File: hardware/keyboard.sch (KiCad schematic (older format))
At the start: 19 parts, among them J1 USB_OTG, J2 CONN_02X10, U1 ATMEGA32U4-AU, Y1 16MHz

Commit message: Update parts after starting sourcing
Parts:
- D101: footprint LEDs:LED_RGB_5050-6 -> LEDs:LED_RGB_PLCC-6
- Y1: footprint Crystals:Crystal_SMD_2012-2pin_2.0x1.2mm_HandSoldering -> Crystals:Crystal_SMD_3225-4pin_3.2x2.5mm_HandSoldering
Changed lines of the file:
@@
 F 0 "Y1" H 2600 1950 50  0000 C CNN
 F 1 "16MHz" H 2600 1750 50  0000 C CNN
-F 2 "Crystals:Crystal_SMD_2012-2pin_2.0x1.2mm_HandSoldering" H 2600 1850 50  0001 C CNN
+F 2 "Crystals:Crystal_SMD_3225-4pin_3.2x2.5mm_HandSoldering" H 2600 1850 50  0001 C CNN
 F 3 "" H 2600 1850 50  0001 C CNN
 	1    2600 1850
@@
 F 0 "D101" H 6900 2097 50  0000 C CNN
 F 1 "LED_RGB" H 6900 2006 50  0000 C CNN
-F 2 "LEDs:LED_RGB_5050-6" H 6900 1550 50  0001 C CNN
+F 2 "LEDs:LED_RGB_PLCC-6" H 6900 1550 50  0001 C CNN
 F 3 "" H 6900 1550 50  0001 C CNN
 	1    6900 1600

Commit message: WIP for V2 fixes
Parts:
- removed J2: CONN_02X10, keyboard-modules:ExpansionPads, symbol CONN_02X10
- added J10, J11, J12, J13, J14, J2, J3, J4, J5, J6, J7, J8, J9: CONN_01X01, keyboard-modules:CONN_1, symbol CONN_01X01
- J1: footprint Connectors_USB:USB_Micro-B_Molex-105017-0001 -> keyboard-modules:USB-MINI
- Y1: footprint Crystals:Crystal_SMD_3225-4pin_3.2x2.5mm_HandSoldering -> Crystals:Crystal_Round_d1.0mm_Vertical
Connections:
- net labels removed: VCC
- wire segments 44 -> 40

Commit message: More WIP on V2
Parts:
- F1: footprint Fuse_Holders_and_Fuses:Fuse_SMD1206_HandSoldering -> Resistors_SMD:R_1206_HandSoldering
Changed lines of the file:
@@
 LIBS:valves
 LIBS:keyboard-cache
-EELAYER 25 0
+EELAYER 26 0
 EELAYER END
 $Descr A4 11693 8268
@@
 F 0 "F1" V 1975 2500 50  0000 C CNN
 F 1 "Polyfuse_Small" V 2125 2500 50  0000 C CNN
-F 2 "Fuse_Holders_and_Fuses:Fuse_SMD1206_HandSoldering" H 2100 2300 50  0001 L CNN
+F 2 "Resistors_SMD:R_1206_HandSoldering" H 2100 2300 50  0001 L CNN
 F 3 "" H 2050 2500 50  0001 C CNN
 	1    2050 2500

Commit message: Add more mounting holes, re-route updated components
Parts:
- removed D101: LED_RGB, LEDs:LED_RGB_PLCC-6, symbol LED_RGB
- removed J10, J11, J12, J13, J14, J2, J3, J4, J5, J6, J8, J9: CONN_01X01, keyboard-modules:CONN_1, symbol CONN_01X01
- removed R1, R3: 1k, Resistors_SMD:R_1206_HandSoldering, symbol R
- added D65: LED_CRGB, LEDs:LED_D5.0mm-4, symbol LED_CRGB
- added GND1, PD2, PD3, PD4, PD5, PD6, PE6, PF0, PF1, PF4, PF5, PF6, PF7, SCL1, SDA1, VCC1: CONN_01X01, keyboard-modules:CONN_1, symbol CONN_01X01
- renumbered J7 to PB7
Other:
- moved on the sheet: PB7

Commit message: finish V2
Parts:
- removed D65: LED_CRGB, LEDs:LED_D5.0mm-4, symbol LED_CRGB
- added D99: LED_ARGB, LEDs:LED_D5.0mm-4-v2, symbol LED_ARGB
- added R1, R3: 1k, Resistors_SMD:R_1206_HandSoldering, symbol R
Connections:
- net +5V: now also D99.1 (A)
- net GND: no longer R2.2
- net LED1: now also R1.2
- net LED2: now also R2.2
- net LED3: now also R3.2
- net at R2.1: now also D99.3 (GK)
- new net: D99.2 (RK), R1.1
- new net: D99.4 (BK), R3.1
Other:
- moved on the sheet: R2
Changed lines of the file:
@@
-$EndComp
-$Comp
-L GND #PWR08
-U 1 1 594E9E01
-P 6400 1600
-F 0 "#PWR08" H 6400 1350 50  0001 C CNN
-F 1 "GND" H 6400 1450 50  0000 C CNN
-F 2 "" H 6400 1600 50  0001 C CNN
-F 3 "" H 6400 1600 50  0001 C CNN
-	1    6400 1600
-	1    0    0    -1
 $EndComp
 $Comp
 L R R2
 U 1 1 594E9E0D
-P 6550 1600
-F 0 "R2" V 6630 1600 50  0000 C CNN
-F 1 "1k" V 6550 1600 50  0000 C CNN
-F 2 "Resistors_SMD:R_1206_HandSoldering" V 6480 1600 50  0001 C CNN
-F 3 "" H 6550 1600 50  0001 C CNN
-	1    6550 1600
+P 6050 1250
+F 0 "R2" V 6130 1250 50  0000 C CNN
+F 1 "1k" V 6050 1250 50  0000 C CNN
+F 2 "Resistors_SMD:R_1206_HandSoldering" V 5980 1250 50  0001 C CNN
+F 3 "" H 6050 1250 50  0001 C CNN
+	1    6050 1250
 	0    1    1    0
 $EndComp
-Text GLabel 7100 1400 2    60   Input ~ 0
+Text GLabel 5900 1050 0    60   Input ~ 0
 LED1
-Text GLabel 7100 1600 2    60   Input ~ 0
+Text GLabel 5900 1250 0    60   Input ~ 0
 LED2
 $Comp
@@
 	5050 3450 5250 3450
 $Comp
-L GND #PWR09
+L GND #PWR08
 U 1 1 594EA1C7
 P 6150 3450
-F 0 "#PWR09" H 6150 3200 50  0001 C CNN
+F 0 "#PWR08" H 6150 3200 50  0001 C CNN
 F 1 "GND" H 6150 3300 50  0000 C CNN
 F 2 "" H 6150 3450 50  0001 C CNN
@@
 	5550 3450 6150 3450
 $Comp
-L GND #PWR010
+L GND #PWR09
 U 1 1 594EA3EB
 P 2050 1350
-F 0 "#PWR010" H 2050 1100 50  0001 C CNN
+F 0 "#PWR09" H 2050 1100 50  0001 C CNN
 F 1 "GND" H 2050 1200 50  0000 C CNN
 F 2 "" H 2050 1350 50  0001 C CNN
@@
 $EndComp
 $Comp
-L +5V #PWR011
+L +5V #PWR010
 U 1 1 5955BD4A
 P 1800 800
-F 0 "#PWR011" H 1800 650 50  0001 C CNN
+F 0 "#PWR010" H 1800 650 50  0001 C CNN
 F 1 "+5V" H 1800 940 50  0000 C CNN
 F 2 "" H 1800 800 50  0001 C CNN
@@
 $EndComp
 $Comp
-L GND #PWR012
+L GND #PWR011
 U 1 1 5955BE42
 P 1800 1000
-F 0 "#PWR012" H 1800 750 50  0001 C CNN
+F 0 "#PWR011" H 1800 750 50  0001 C CNN
 F 1 "GND" H 1800 850 50  0000 C CNN
 F 2 "" H 1800 1000 50  0001 C CNN
@@
 	1    0    0    -1
 $EndComp
-Text GLabel 7100 1800 2    60   Input ~ 0
+Text GLabel 5900 1450 0    60   Input ~ 0
 LED3
 Text GLabel 5050 1850 2    60   Input ~ 0
@@
 $EndComp
 $Comp
-L LED_CRGB D65
-U 1 1 5A0960D5
-P 6900 1600
-F 0 "D65" H 6900 1970 50  0000 C CNN
-F 1 "LED_CRGB" H 6900 1250 50  0000 C CNN
-F 2 "LEDs:LED_D5.0mm-4" H 6900 1550 50  0001 C CNN
-F 3 "" H 6900 1550 50  0001 C CNN
-	1    6900 1600
-	1    0    0    -1
-$EndComp
-$Comp
 L CONN_01X01 PD6
 U 1 1 5A09791E
@@
 	1    0    0    -1
 $EndComp
-Connection ~ 9450 2350
 Connection ~ 5600 2450
+$Comp
+L LED_ARGB D99
+U 1 1 5A1A0698
+P 6400 1250
+F 0 "D99" H 6400 1620 50  0000 C CNN
+F 1 "LED_ARGB" H 6400 900 50  0000 C CNN
+F 2 "LEDs:LED_D5.0mm-4-v2" H 6400 1200 50  0001 C CNN
+F 3 "" H 6400 1200 50  0001 C CNN
+	1    6400 1250
+	1    0    0    -1
+$EndComp
+$Comp
+L R R1
+U 1 1 5A1A082F
+P 6050 1050
+F 0 "R1" V 6130 1050 50  0000 C CNN
+F 1 "1k" V 6050 1050 50  0000 C CNN
+F 2 "Resistors_SMD:R_1206_HandSoldering" V 5980 1050 50  0001 C CNN
+F 3 "" H 6050 1050 50  0001 C CNN
+	1    6050 1050
+	0    1    1    0
+$EndComp
+$Comp
+L R R3
+U 1 1 5A1A08BC
+P 6050 1450
+F 0 "R3" V 6130 1450 50  0000 C CNN
+F 1 "1k" V 6050 1450 50  0000 C CNN
+F 2 "Resistors_SMD:R_1206_HandSoldering" V 5980 1450 50  0001 C CNN
+F 3 "" H 6050 1450 50  0001 C CNN
+	1    6050 1450
+	0    1    1    0
+$EndComp
+$Comp
+L +5V #PWR012
+U 1 1 5A1A091A
+P 6600 1250
+F 0 "#PWR012" H 6600 1100 50  0001 C CNN
+F 1 "+5V" H 6600 1390 50  0000 C CNN
+F 2 "" H 6600 1250 50  0001 C CNN
+F 3 "" H 6600 1250 50  0001 C CNN
+	1    6600 1250
+	1    0    0    -1
+$EndComp
 $EndSCHEMATC

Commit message: Update schematic, WIP fixes + adding test points
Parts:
- removed GND1, PB7, PD2, PD3, PD4, PD5, PD6, PE6, PF0, PF1, PF4, PF5, PF6, PF7, SCL1, SDA1, VCC1: CONN_01X01, keyboard-modules:CONN_1, symbol CONN_01X01
- added J2: CONN_01X05, Pin_Headers:Pin_Header_Straight_1x05_Pitch1.27mm, symbol CONN_01X05
- added J3: CONN_01X04, Pin_Headers:Pin_Header_Straight_1x04_Pitch1.27mm, symbol CONN_01X04
- added J4: CONN_01X07, Pin_Headers:Pin_Header_Straight_1x07_Pitch1.27mm, symbol CONN_01X07
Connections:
- net +5V: now also J3.1 (P1), J4.1 (P1)
- net GND: now also J3.4 (P4), J4.7 (P7)
- net LED1: now also U1.28 ((ADC11/PCINT4)PB4); no longer U1.29 ((ADC12/OC1A/~OC4B~/PCINT12)PB5)
- net LED2: now also U1.29 ((ADC12/OC1A/~OC4B~/PCINT12)PB5); no longer U1.30 ((ADC13/OC1B/OC4B/PCINT13)PB6)
- net LED3: now also U1.30 ((ADC13/OC1B/OC4B/PCINT13)PB6); no longer U1.27 ((T0/OC4D/ADC10)PD7)
- net PF4: now also J4.3 (P3)
- net PF5: now also J4.4 (P4)
- net PF6: now also J4.5 (P5)
- net PF7: now also J4.6 (P6)
- net ROW0: now also J2.1 (P1)
- net ROW1: now also J2.2 (P2)
- net ROW2: now also J2.3 (P3)
- net ROW3: now also J2.4 (P4)
- net ROW4: now also U1.12 ((OC0A/OC1C/~RTS~/PCINT7)PB7), J2.5 (P5); no longer U1.28 ((ADC11/PCINT4)PB4)
- net SCL: now also J3.2 (P2)
- net SDA: now also J3.3 (P3)
- net RESET: now reaches S100.2, U1.13 (~RESET~)
- net RESET: now also J4.2 (P2)
- net PE2: now reaches R8.2, U1.33 ((~HWB~)PE2)
- new net PD7: U1.27 ((T0/OC4D/ADC10)PD7)
- no-connect marks 0 -> 3
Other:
- moved on the sheet: R4, R5, S100

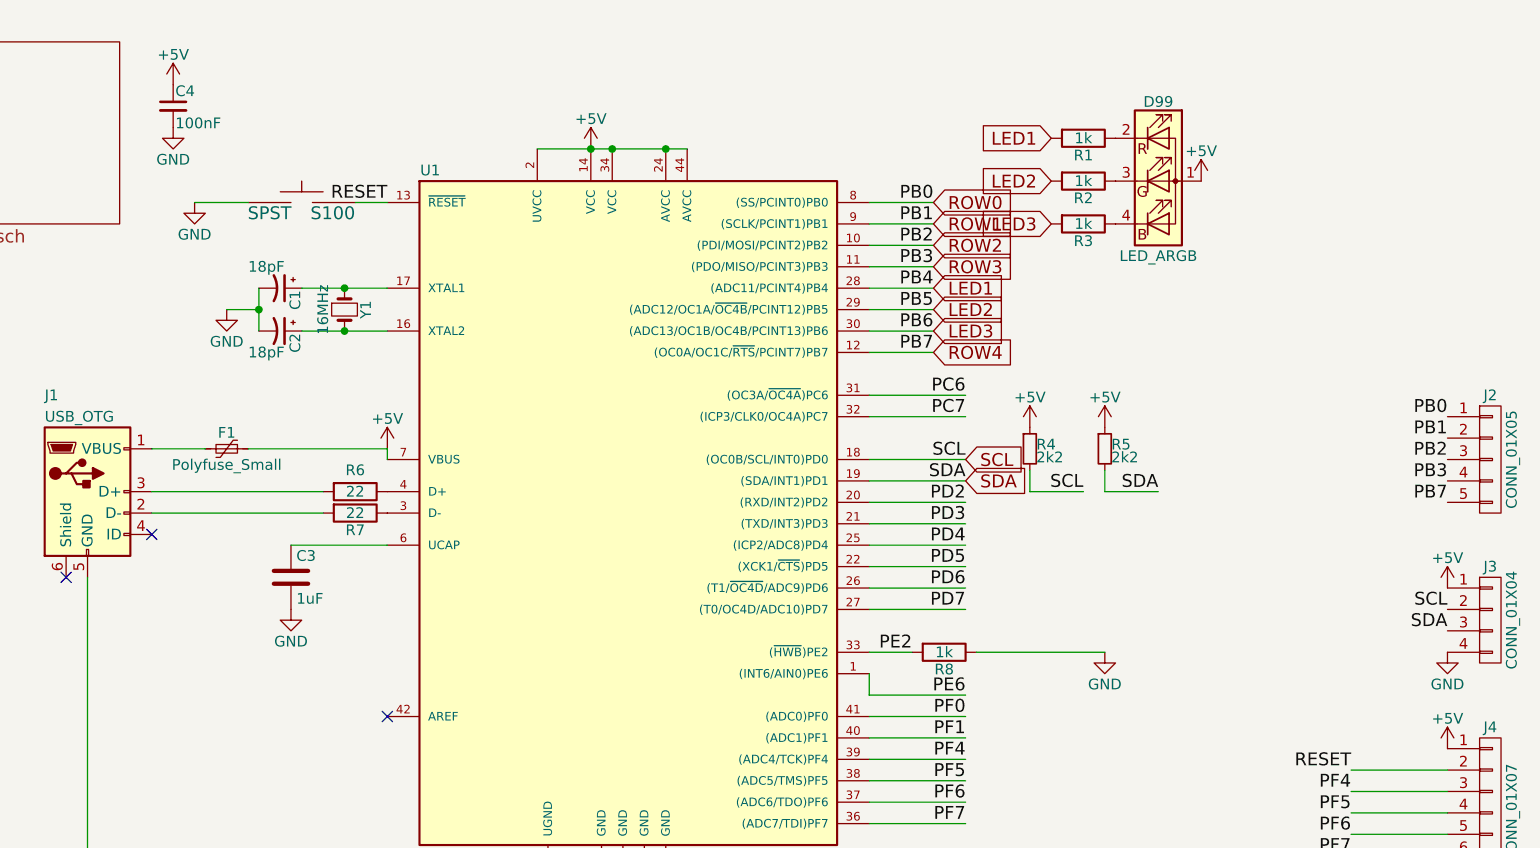
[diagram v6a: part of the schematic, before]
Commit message: PCB revisions - more test points and fixes
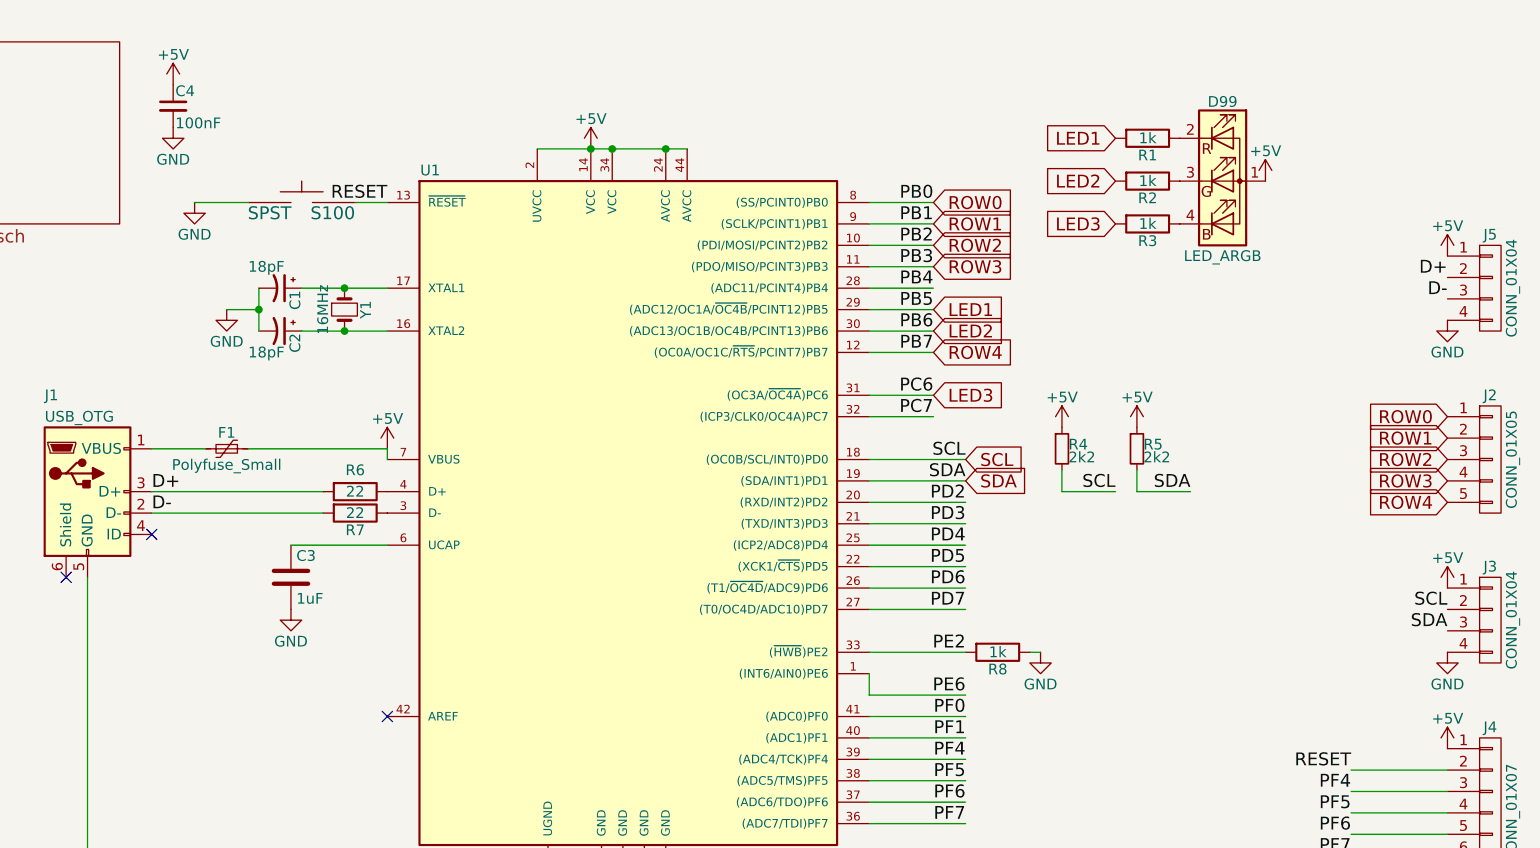
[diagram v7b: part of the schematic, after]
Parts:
- added J5: CONN_01X04, Pin_Headers:Pin_Header_Straight_1x04_Pitch1.27mm, symbol CONN_01X04
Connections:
- net PC6 is gone; now on net LED3: U1.31 ((OC3A/~OC4A~)PC6)
- net +5V: now also J5.1 (P1)
- net GND: now also J5.4 (P4)
- net LED1: now also U1.29 ((ADC12/OC1A/~OC4B~/PCINT12)PB5); no longer U1.28 ((ADC11/PCINT4)PB4)
- net LED2: now also U1.30 ((ADC13/OC1B/OC4B/PCINT13)PB6); no longer U1.29 ((ADC12/OC1A/~OC4B~/PCINT12)PB5)
- net LED3: no longer U1.30 ((ADC13/OC1B/OC4B/PCINT13)PB6)
- net D-: now reaches J1.2 (D-), R7.2
- net D-: now also J5.3 (P3)
- net D+: now reaches J1.3 (D+), R6.2
- net D+: now also J5.2 (P2)
- new net PB4: U1.28 ((ADC11/PCINT4)PB4)
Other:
- moved on the sheet: D99, R1, R2, R3, R4, R5, R8
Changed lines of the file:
@@
 EESchema Schematic File Version 2
-LIBS:keyboard-rescue
 LIBS:power
 LIBS:device
@@
 L R_Small R5
 U 1 1 594E97F5
-P 6150 2500
-F 0 "R5" H 6180 2520 50  0000 L CNN
-F 1 "2k2" H 6180 2460 50  0000 L CNN
-F 2 "Resistors_SMD:R_1206_HandSoldering" H 6150 2500 50  0001 C CNN
-F 3 "" H 6150 2500 50  0001 C CNN
-	1    6150 2500
+P 6300 2500
+F 0 "R5" H 6330 2520 50  0000 L CNN
+F 1 "2k2" H 6330 2460 50  0000 L CNN
+F 2 "Resistors_SMD:R_1206_HandSoldering" H 6300 2500 50  0001 C CNN
+F 3 "" H 6300 2500 50  0001 C CNN
+	1    6300 2500
 	1    0    0    -1
 $EndComp
@@
 L R_Small R4
 U 1 1 594E9840
-P 5800 2500
-F 0 "R4" H 5830 2520 50  0000 L CNN
-F 1 "2k2" H 5830 2460 50  0000 L CNN
-F 2 "Resistors_SMD:R_1206_HandSoldering" H 5800 2500 50  0001 C CNN
-F 3 "" H 5800 2500 50  0001 C CNN
-	1    5800 2500
+P 5950 2500
+F 0 "R4" H 5980 2520 50  0000 L CNN
+F 1 "2k2" H 5980 2460 50  0000 L CNN
+F 2 "Resistors_SMD:R_1206_HandSoldering" H 5950 2500 50  0001 C CNN
+F 3 "" H 5950 2500 50  0001 C CNN
+	1    5950 2500
 	1    0    0    -1
 $EndComp
@@
 L +5V #PWR06
 U 1 1 594E98E9
-P 5800 2400
-F 0 "#PWR06" H 5800 2250 50  0001 C CNN
-F 1 "+5V" H 5800 2540 50  0000 C CNN
-F 2 "" H 5800 2400 50  0001 C CNN
-F 3 "" H 5800 2400 50  0001 C CNN
-	1    5800 2400
+P 5950 2400
+F 0 "#PWR06" H 5950 2250 50  0001 C CNN
+F 1 "+5V" H 5950 2540 50  0000 C CNN
+F 2 "" H 5950 2400 50  0001 C CNN
+F 3 "" H 5950 2400 50  0001 C CNN
+	1    5950 2400
 	1    0    0    -1
 $EndComp
@@
 L +5V #PWR07
 U 1 1 594E9917
-P 6150 2400
-F 0 "#PWR07" H 6150 2250 50  0001 C CNN
-F 1 "+5V" H 6150 2540 50  0000 C CNN
-F 2 "" H 6150 2400 50  0001 C CNN
-F 3 "" H 6150 2400 50  0001 C CNN
-	1    6150 2400
+P 6300 2400
+F 0 "#PWR07" H 6300 2250 50  0001 C CNN
+F 1 "+5V" H 6300 2540 50  0000 C CNN
+F 2 "" H 6300 2400 50  0001 C CNN
+F 3 "" H 6300 2400 50  0001 C CNN
+	1    6300 2400
 	1    0    0    -1
 $EndComp
@@
 L R R2
 U 1 1 594E9E0D
-P 6050 1250
-F 0 "R2" V 6130 1250 50  0000 C CNN
-F 1 "1k" V 6050 1250 50  0000 C CNN
-F 2 "Resistors_SMD:R_1206_HandSoldering" V 5980 1250 50  0001 C CNN
-F 3 "" H 6050 1250 50  0001 C CNN
-	1    6050 1250
-	0    1    1    0
-$EndComp
-Text GLabel 5900 1050 0    60   Input ~ 0
+P 6350 1250
+F 0 "R2" V 6430 1250 50  0000 C CNN
+F 1 "1k" V 6350 1250 50  0000 C CNN
+F 2 "Resistors_SMD:R_1206_HandSoldering" V 6280 1250 50  0001 C CNN
+F 3 "" H 6350 1250 50  0001 C CNN
+	1    6350 1250
+	0    1    1    0
+$EndComp
+Text GLabel 6200 1050 0    60   Input ~ 0
 LED1
-Text GLabel 5900 1250 0    60   Input ~ 0
+Text GLabel 6200 1250 0    60   Input ~ 0
 LED2
 $Comp
 L R R8
 U 1 1 594EA13B
-P 5400 3450
-F 0 "R8" V 5480 3450 50  0000 C CNN
-F 1 "1k" V 5400 3450 50  0000 C CNN
-F 2 "Resistors_SMD:R_1206_HandSoldering" V 5330 3450 50  0001 C CNN
-F 3 "" H 5400 3450 50  0001 C CNN
-	1    5400 3450
-	0    1    1    0
-$EndComp
-Wire Wire Line
-	5050 3450 5250 3450
+P 5650 3450
+F 0 "R8" V 5730 3450 50  0000 C CNN
+F 1 "1k" V 5650 3450 50  0000 C CNN
+F 2 "Resistors_SMD:R_1206_HandSoldering" V 5580 3450 50  0001 C CNN
+F 3 "" H 5650 3450 50  0001 C CNN
+	1    5650 3450
+	0    1    1    0
+$EndComp
+Wire Wire Line
+	5050 3450 5500 3450
 $Comp
 L GND #PWR08
 U 1 1 594EA1C7
-P 6150 3450
-F 0 "#PWR08" H 6150 3200 50  0001 C CNN
-F 1 "GND" H 6150 3300 50  0000 C CNN
-F 2 "" H 6150 3450 50  0001 C CNN
-F 3 "" H 6150 3450 50  0001 C CNN
-	1    6150 3450
-	1    0    0    -1
-$EndComp
-Wire Wire Line
-	5550 3450 6150 3450
+P 5850 3450
+F 0 "#PWR08" H 5850 3200 50  0001 C CNN
+F 1 "GND" H 5850 3300 50  0000 C CNN
+F 2 "" H 5850 3450 50  0001 C CNN
+F 3 "" H 5850 3450 50  0001 C CNN
+	1    5850 3450
+	1    0    0    -1
+$EndComp
+Wire Wire Line
+	5800 3450 5850 3450
 $Comp
 L GND #PWR09
@@
 	2150 1350 1900 1350
 Wire Wire Line
-	5050 2250 5500 2250
-Wire Wire Line
-	5050 2350 5500 2350
-Wire Wire Line
 	5050 2750 5500 2750
 Wire Wire Line
@@
 Wire Wire Line
 	7300 4400 7750 4400
-Text Label 5500 2250 2    60   ~ 0
+Text Label 5350 2250 2    60   ~ 0
 PC6
-Text Label 5500 2350 2    60   ~ 0
+Text Label 5350 2350 2    60   ~ 0
 PC7
 Text Label 5500 2750 2    60   ~ 0
@@
 	1    0    0    -1
 $EndComp
-Text GLabel 5900 1450 0    60   Input ~ 0
+Text GLabel 6200 1450 0    60   Input ~ 0
 LED3
-Text GLabel 5350 1750 2    60   Input ~ 0
+Text GLabel 5350 1850 2    60   Input ~ 0
 LED1
-Text GLabel 5350 1850 2    60   Input ~ 0
+Text GLabel 5350 1950 2    60   Input ~ 0
 LED2
-Text GLabel 5350 1950 2    60   Input ~ 0
+Text GLabel 5350 2250 2    60   Input ~ 0
 LED3
 $Comp
 L LED_ARGB D99
 U 1 1 5A1A0698
-P 6400 1250
-F 0 "D99" H 6400 1620 50  0000 C CNN
-F 1 "LED_ARGB" H 6400 900 50  0000 C CNN
-F 2 "LEDs:LED_D5.0mm-4-v2" H 6400 1200 50  0001 C CNN
-F 3 "" H 6400 1200 50  0001 C CNN
-	1    6400 1250
+P 6700 1250
+F 0 "D99" H 6700 1620 50  0000 C CNN
+F 1 "LED_ARGB" H 6700 900 50  0000 C CNN
+F 2 "LEDs:LED_D5.0mm-4-v2" H 6700 1200 50  0001 C CNN
+F 3 "" H 6700 1200 50  0001 C CNN
+	1    6700 1250
 	1    0    0    -1
 $EndComp
@@
 L R R1
 U 1 1 5A1A082F
-P 6050 1050
-F 0 "R1" V 6130 1050 50  0000 C CNN
-F 1 "1k" V 6050 1050 50  0000 C CNN
-F 2 "Resistors_SMD:R_1206_HandSoldering" V 5980 1050 50  0001 C CNN
-F 3 "" H 6050 1050 50  0001 C CNN
-	1    6050 1050
+P 6350 1050
+F 0 "R1" V 6430 1050 50  0000 C CNN
+F 1 "1k" V 6350 1050 50  0000 C CNN
+F 2 "Resistors_SMD:R_1206_HandSoldering" V 6280 1050 50  0001 C CNN
+F 3 "" H 6350 1050 50  0001 C CNN
+	1    6350 1050
 	0    1    1    0
 $EndComp
@@
 L R R3
 U 1 1 5A1A08BC
-P 6050 1450
-F 0 "R3" V 6130 1450 50  0000 C CNN
-F 1 "1k" V 6050 1450 50  0000 C CNN
-F 2 "Resistors_SMD:R_1206_HandSoldering" V 5980 1450 50  0001 C CNN
-F 3 "" H 6050 1450 50  0001 C CNN
-	1    6050 1450
+P 6350 1450
+F 0 "R3" V 6430 1450 50  0000 C CNN
+F 1 "1k" V 6350 1450 50  0000 C CNN
+F 2 "Resistors_SMD:R_1206_HandSoldering" V 6280 1450 50  0001 C CNN
+F 3 "" H 6350 1450 50  0001 C CNN
+	1    6350 1450
 	0    1    1    0
 $EndComp
@@
 L +5V #PWR012
 U 1 1 5A1A091A
-P 6600 1250
-F 0 "#PWR012" H 6600 1100 50  0001 C CNN
-F 1 "+5V" H 6600 1390 50  0000 C CNN
-F 2 "" H 6600 1250 50  0001 C CNN
-F 3 "" H 6600 1250 50  0001 C CNN
-	1    6600 1250
+P 6900 1250
+F 0 "#PWR012" H 6900 1100 50  0001 C CNN
+F 1 "+5V" H 6900 1390 50  0000 C CNN
+F 2 "" H 6900 1250 50  0001 C CNN
+F 3 "" H 6900 1250 50  0001 C CNN
+	1    6900 1250
 	1    0    0    -1
 $EndComp
@@
 Text Label 5500 3950 2    60   ~ 0
 PF4
-Text Label 5250 3450 2    60   ~ 0
+Text Label 5500 3450 2    60   ~ 0
 PE2
 Wire Wire Line
@@
 SDA
 Wire Wire Line
-	5800 2600 5800 2700
-Wire Wire Line
-	5800 2700 6050 2700
-Text Label 6050 2700 2    60   ~ 0
+	5950 2600 5950 2700
+Wire Wire Line
+	5950 2700 6200 2700
+Text Label 6200 2700 2    60   ~ 0
 SCL
 Wire Wire Line
-	6400 2700 6150 2700
-Wire Wire Line
-	6150 2700 6150 2600
-Text Label 6400 2700 2    60   ~ 0
+	6550 2700 6300 2700
+Wire Wire Line
+	6300 2700 6300 2600
+Text Label 6550 2700 2    60   ~ 0
 SDA
 Wire Wire Line
@@
 	1    0    0    -1
 $EndComp
-Text Label 7750 2350 2    60   ~ 0
-PB0
-Text Label 7750 2450 2    60   ~ 0
-PB1
-Text Label 7750 2550 2    60   ~ 0
-PB2
-Text Label 7750 2650 2    60   ~ 0
-PB3
-Text Label 7750 2750 2    60   ~ 0
-PB7
 NoConn ~ 1700 2900
 NoConn ~ 1300 3100
@@
 Wire Wire Line
 	2650 1350 2800 1350
+$Comp
+L CONN_01X04 J5
+U 1 1 5A2C2586
+P 7950 1750
+F 0 "J5" H 7950 2000 50  0000 C CNN
+F 1 "CONN_01X04" V 8050 1750 50  0000 C CNN
+F 2 "Pin_Headers:Pin_Header_Straight_1x04_Pitch1.27mm" H 7950 1750 50  0001 C CNN
+F 3 "" H 7950 1750 50  0001 C CNN
+	1    7950 1750
+	1    0    0    -1
+$EndComp
+$Comp
+L +5V #PWR017
+U 1 1 5A2C2674
+P 7750 1600
+F 0 "#PWR017" H 7750 1450 50  0001 C CNN
+F 1 "+5V" H 7750 1740 50  0000 C CNN
+F 2 "" H 7750 1600 50  0001 C CNN
+F 3 "" H 7750 1600 50  0001 C CNN
+	1    7750 1600
+	1    0    0    -1
+$EndComp
+$Comp
+L GND #PWR018
+U 1 1 5A2C26B4
+P 7750 1900
+F 0 "#PWR018" H 7750 1650 50  0001 C CNN
+F 1 "GND" H 7750 1750 50  0000 C CNN
+F 2 "" H 7750 1900 50  0001 C CNN
+F 3 "" H 7750 1900 50  0001 C CNN
+	1    7750 1900
+	1    0    0    -1
+$EndComp
+Text Label 7750 1700 2    60   ~ 0
+D+
+Text Label 7750 1800 2    60   ~ 0
+D-
+Text Label 1700 2700 0    60   ~ 0
+D+
+Text Label 1700 2800 0    60   ~ 0
+D-
+Wire Wire Line
+	5050 2250 5350 2250
+Wire Wire Line
+	5350 2350 5050 2350
+Text GLabel 7750 2350 0    60   Input ~ 0
+ROW0
+Text GLabel 7750 2450 0    60   Input ~ 0
+ROW1
+Text GLabel 7750 2550 0    60   Input ~ 0
+ROW2
+Text GLabel 7750 2650 0    60   Input ~ 0
+ROW3
+Text GLabel 7750 2750 0    60   Input ~ 0
+ROW4
 $EndSCHEMATC
